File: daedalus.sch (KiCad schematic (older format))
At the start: 45 parts

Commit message: Updated schematic with MPU6050
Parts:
- added C?: 0.1uF, symbol Device:C_Small
- added C?: 2.2nF, symbol Device:C_Small
- added C? (x2): 100nF, symbol Device:C_Small
- added D?: Blue, LED_SMD:LED_0603_1608Metric, symbol Device:LED_Small
- added D?: Green, LED_SMD:LED_0603_1608Metric, symbol Device:LED_Small
- added J?: JST LiPo Input, symbol Connector:Screw_Terminal_01x02
- added J?: I2C 1 Breakout, symbol Connector_Generic:Conn_01x04
- added J? (x2): Conn_01x20_Male, symbol Connector:Conn_01x20_Male
- added R?: 1k, Resistor_SMD:R_0402_1005Metric, symbol Device:R_Small
- added R?: 1k5, Resistor_SMD:R_0402_1005Metric, symbol Device:R_Small
- added U?: MPU-6050, Sensor_Motion:InvenSense_QFN-24_4x4mm_P0.5mm, symbol Sensor_Motion:MPU-6050
- C?: value 100 nF -> 1uF
- C?: value 10 nF -> 10nF
- F?: value 500mA -> 250mA
- FB?: value 100 @ 100 MHz -> 600 @ 600MHz
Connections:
- net labels added: INT_ACC, INT_GYR, MPU_INT
- wire segments 82 -> 97
- no-connect marks 4 -> 6
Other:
- note added: "Inertial Measurement Unit"
- note added: "Pinout Connections"
- moved on the sheet: C?, D?, FB?, H?, L?, R?, SW?

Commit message: Added footprints and side headers
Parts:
- C1, C13, C14, C2, C20, C3, C4: renamed from C?; footprint (none) -> Capacitor_SMD:C_0402_1005Metric
- C19: renamed from C?; value 0.1uF -> 100nF; footprint (none) -> Capacitor_SMD:C_0402_1005Metric
- D1, D2: renamed from D?; footprint (none) -> Diode_SMD:D_SOD-123
- F1: renamed from F?; footprint (none) -> Fuse:Fuse_0603_1608Metric
- FB1: renamed from FB?; footprint (none) -> Inductor_SMD:L_0805_2012Metric
- H1, H2, H3, H4: renamed from H?; footprint (none) -> MountingHole:MountingHole_2.7mm_M2.5_Pad
- J1: renamed from J?; footprint (none) -> Connector_PinHeader_1.27mm:PinHeader_2x05_P1.27mm_Vertical_SMD
- J2: renamed from J?; footprint (none) -> Connector_USB:USB_Micro-AB_Molex_47590-0001
- J3: renamed from J?; footprint (none) -> Connector_JST:JST_PH_S2B-PH-K_1x02_P2.00mm_Horizontal
- J4: renamed from J?; footprint (none) -> Eric:JST_SH4
- J5, J6: renamed from J?; footprint (none) -> Connector_PinHeader_2.54mm:PinHeader_1x20_P2.54mm_Vertical
- L1: renamed from L?; footprint (none) -> Inductor_SMD:L_0603_1608Metric
- R1, R2, R3, R4, R5: renamed from R?; footprint (none) -> Resistor_SMD:R_0402_1005Metric
- U1: renamed from U?; footprint (none) -> Package_TO_SOT_SMD:SOT-23-6
- gave numbers to parts that had none: 29
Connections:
- net labels added: GPDIO_PC12, GPIO_PA0, GPIO_PA1, GPIO_PA10, GPIO_PA15, GPIO_PA2, GPIO_PA3, GPIO_PA4, GPIO_PA8, GPIO_PA9, GPIO_PB0, GPIO_PB1, GPIO_PB12, GPIO_PB13, GPIO_PB14, GPIO_PB15, GPIO_PB2, GPIO_PB4, GPIO_PB5, GPIO_PB8, GPIO_PB9, GPIO_PC0, GPIO_PC1, GPIO_PC10, GPIO_PC11, GPIO_PC12, GPIO_PC13, GPIO_PC14, GPIO_PC15, GPIO_PC2, GPIO_PC3, GPIO_PC4, GPIO_PC6, GPIO_PC7, GPIO_PC8, GPIO_PC9, GPIO_PD2, SPI1_MISO, SPI1_MOSI, SPI1_SCK, SPI_1_MISO, SPI_1_MOSI

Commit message: Began work adding DRV8323
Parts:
- removed C13, C14, C19: 100nF, Capacitor_SMD:C_0402_1005Metric, symbol Device:C_Small
- removed C20: 2.2nF, Capacitor_SMD:C_0402_1005Metric, symbol Device:C_Small
- removed J5, J6: Conn_01x20_Male, Connector_PinHeader_2.54mm:PinHeader_1x20_P2.54mm_Vertical, symbol Connector:Conn_01x20_Male
- removed U3: MPU-6050, Sensor_Motion:InvenSense_QFN-24_4x4mm_P0.5mm, symbol Sensor_Motion:MPU-6050
- added ?: DRV8323RH, symbol drv8323rh:DRV8323RH
- added ?: MA700, symbol ma700:MA700
- added C?: 10uF, symbol Device:C_Small
- added C?: 0.1 uF, symbol Device:C_Small
- added C?: 1 uF, symbol Device:C_Small
- added C?: 47 nF, symbol Device:C_Small
- added C?: C_Small, symbol Device:C_Small
- added C?: 22uF, symbol Device:C_Small
- added C? (x2): 0.1uF, symbol Device:C_Small
- added C?: 1uF, symbol Device:C_Small
- added D?: DIODE, symbol Simulation_SPICE:DIODE
- added L?: 22uH, symbol Device:L_Small
- added R? (x3): 10k, symbol Device:R_Small
- added R?: 54.9k, symbol Device:R_Small
- U1: symbol mp2359dj-lf-z:MP2359DJ-LF-Z -> daedalus-rescue:MP2359DJ-LF-Z-mp2359dj-lf-z
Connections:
- net labels added: +BATT, CAL, CB, ENABLE, END_A, END_B, FAULT, FB, GHA, GHB, GHC, GLA, GLB, GLC, PHASE_A, PHASE_B, PHASE_C, PWM_A, PWM_B, PWM_C, SPA, SPB, SPC, SPI_1_SCK, SPI_2_CS, SPI_2_MISO, SPI_2_MOSI, SPI_2_SCK, SW, VDS
- net labels removed: GPDIO_PC12, GPIO_PA0, GPIO_PA1, GPIO_PA10, GPIO_PA15, GPIO_PA2, GPIO_PA3, GPIO_PA8, GPIO_PA9, GPIO_PB0, GPIO_PB1, GPIO_PB12, GPIO_PB13, GPIO_PB14, GPIO_PB15, GPIO_PB2, GPIO_PB4, GPIO_PB5, GPIO_PB8, GPIO_PB9, GPIO_PC0, GPIO_PC1, GPIO_PC10, GPIO_PC11, GPIO_PC12, GPIO_PC13, GPIO_PC14, GPIO_PC15, GPIO_PC2, GPIO_PC3, GPIO_PC4, GPIO_PC6, GPIO_PC7, GPIO_PC8, GPIO_PC9, GPIO_PD2, INT_ACC, INT_GYR, MPU_INT
- wire segments 97 -> 151
- no-connect marks 6 -> 13
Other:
- note added: "DRV8323"
- note added: "Gate Driver"
- note added: "MA700GQ"
- note added: "Magnetic Encoder"
- note removed: "Inertial Measurement Unit"
- moved on the sheet: J1, J2, J3, J4, U2

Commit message: Added SPI busses, updated CubeMX files
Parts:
- added 3, U3, U5, U6, U7, U8: TPH, symbol tph:TPH
- added C26, C27, C28, C29, C30, C31, C32, C33, C34, C35, C36, C37, C38, C39, C40, C41: 10uF, 50v, symbol Device:C_Small
- added J5, J6, J7: Conn_01x01, symbol Connector_Generic:Conn_01x01
- added R17, R18, R19: 0.001, symbol Device:R_Small
- gave numbers to parts that had none: 17
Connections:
- net GPIO_PA4 is gone; now on net SPI1_NSS: U4.20 (PA4)
- net SPI1_SCK is gone; now on net GND: U4.21 (PA5)
- net SPI_1_MISO is gone; now on net SPI1_MISO: 2.29 (MODE), R13.2
- net SPI_1_MOSI is gone; now on net SPI1_MOSI: 2.30 (IDRIVE)
- net SPI_2_MISO is gone; now on net SPI2_MISO: 1.7 (MISO)
- net SPI_2_MOSI is gone; now on net SPI2_MOSI: 1.4 (MOSI)
- net SPI_2_SCK is gone; now on net SPI2_SCK: 1.12 (SCLK)
- net +BATT: now also C26.1, C27.1, C28.1, C29.1, C30.1, C31.1, C32.1, C33.1, C34.1, C35.1, C36.1, C37.1, C38.1, C39.1, C40.1, C41.1, U3.5 (D), U3.6 (D), U3.7 (D), U3.8 (D), U3.EP (D), U5.5 (D), U5.6 (D), U5.7 (D), U5.8 (D), U5.EP (D), U6.5 (D), U6.6 (D), U6.7 (D), U6.8 (D), U6.EP (D)
- net ENABLE: now also U4.17 (PA3)
- net GHA: now also U3.4 (G)
- net GHB: now also U5.4 (G)
- net GHC: now also U6.4 (G)
- net GLA: now also 3.4 (G)
- net GLB: now also U7.4 (G)
- net GLC: now also U8.4 (G)
- net GND: now also C26.2, C27.2, C28.2, C29.2, C30.2, C31.2, C32.2, C33.2, C34.2, C35.2, C36.2, C37.2, C38.2, C39.2, C40.2, C41.2, R17.2, R18.2, R19.2
- net LED_STATUS: now also U4.50 (PA15); no longer U4.16 (PA2)
- net PHASE_A: now also 3.5 (D), 3.6 (D), 3.7 (D), 3.8 (D), 3.EP (D), J5.1 (Pin_1), U3.1 (S), U3.2 (S), U3.3 (S)
- net PHASE_B: now also J6.1 (Pin_1), U5.1 (S), U5.2 (S), U5.3 (S), U7.5 (D), U7.6 (D), U7.7 (D), U7.8 (D), U7.EP (D)
- net PHASE_C: now also J7.1 (Pin_1), U6.1 (S), U6.2 (S), U6.3 (S), U8.5 (D), U8.6 (D), U8.7 (D), U8.8 (D), U8.EP (D)
- net PWM_A: now also U4.14 (PA0)
- net PWM_B: now also U4.15 (PA1)
- net PWM_C: now also U4.16 (PA2)
- net SPA: now also 3.1 (S), 3.2 (S), 3.3 (S), R17.1
- net SPB: now also R18.1, U7.1 (S), U7.2 (S), U7.3 (S)
- net SPC: now also R19.1, U8.1 (S), U8.2 (S), U8.3 (S)
- net SPI2_MISO: now reaches U4.10 (PC2)
- net SPI2_MOSI: now reaches U4.11 (PC3)
- net SPI2_SCK: now reaches U4.34 (PB13)
- net SPI1_NSS: now reaches 2.32 (GAIN)
- net SPI_2_CS renamed SPI2_CS
- no-connect marks 13 -> 14
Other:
- note added: "DAEDALUS"
- note added: "Motor Interface"
- moved on the sheet: C13, C14, C19, C20, C21, C22, C23, C24, C25, D6, J1, J2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

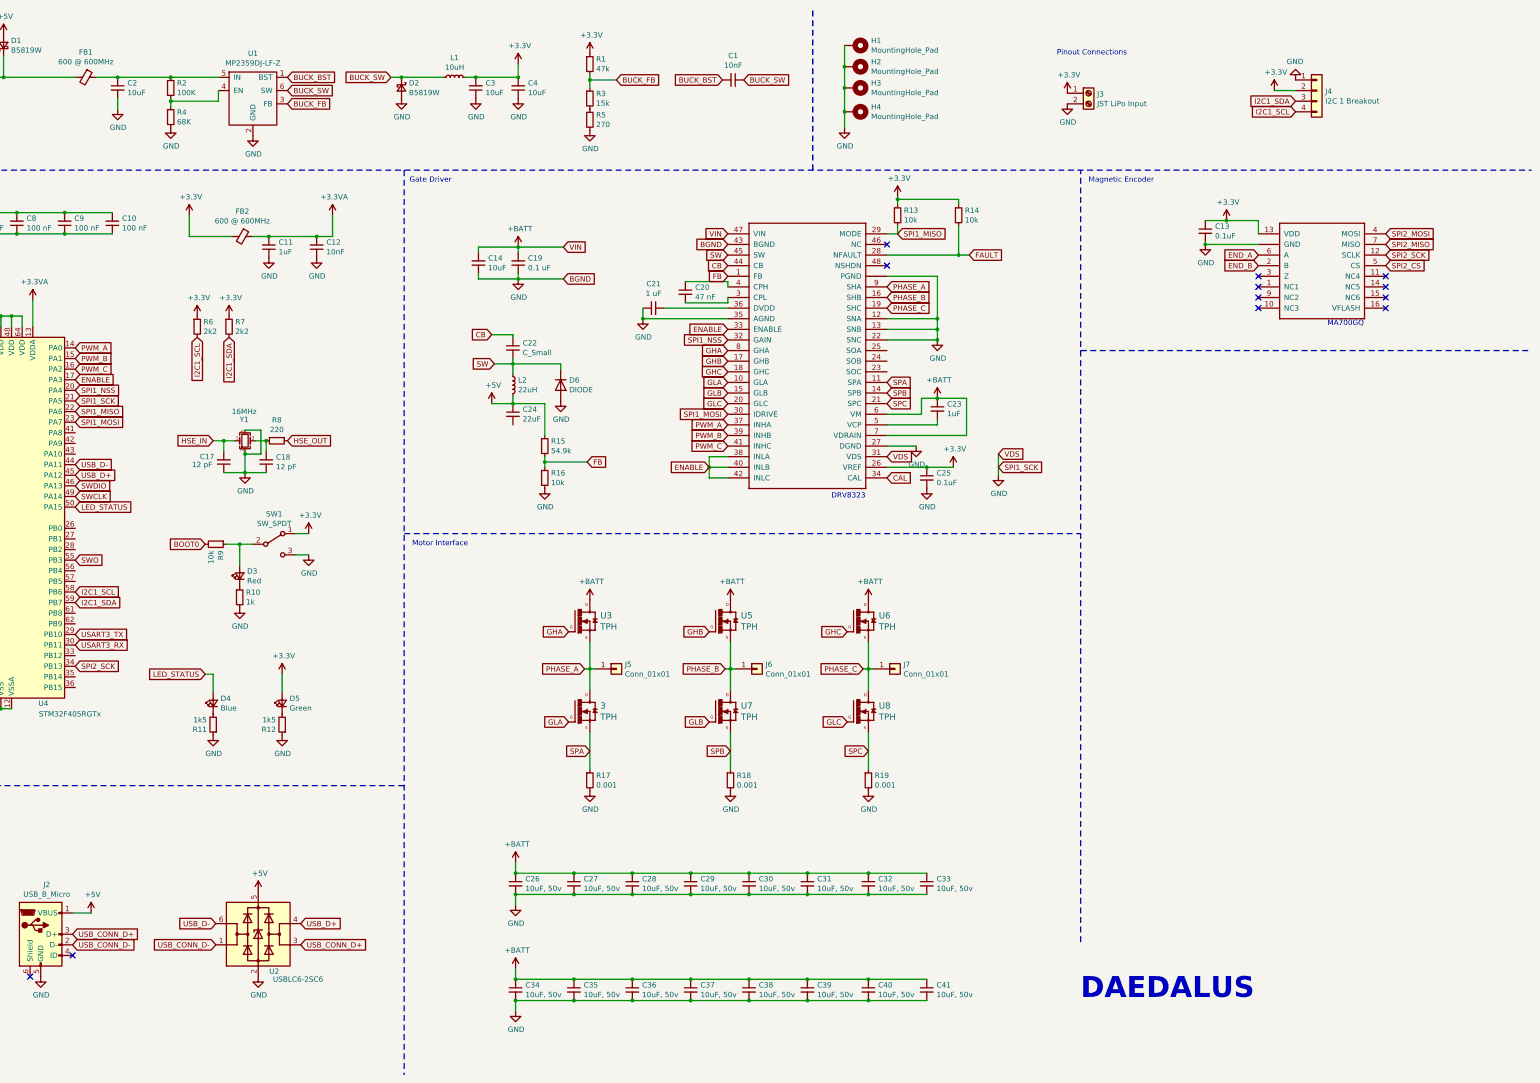
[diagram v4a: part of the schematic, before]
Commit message: Added CAN interface, fixed value labels
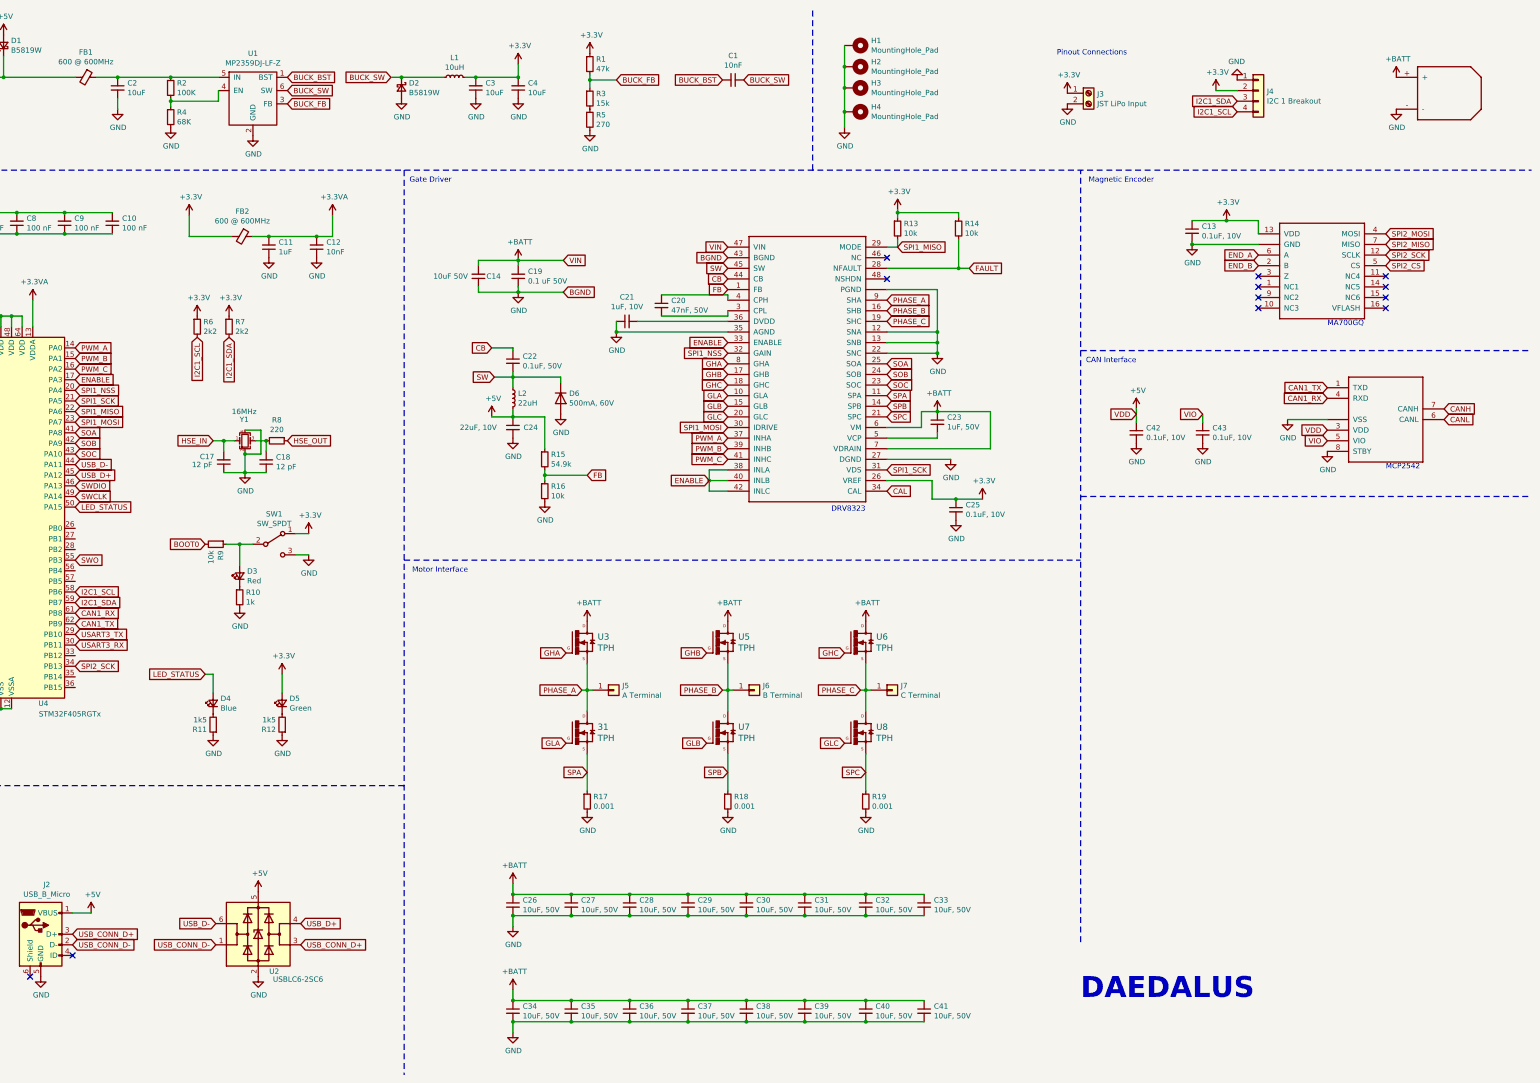
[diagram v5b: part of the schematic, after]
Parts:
- added 1?: XT30, symbol xt30:XT30
- added 2?: MCP2542, symbol mcp2542:MCP2542
- added C42, C43: 0.1uF, 10V, symbol Device:C_Small
- C13, C25: value 0.1uF -> 0.1uF, 10V
- C14: value 10uF -> 10uF 50V
- C19: value 0.1 uF -> 0.1 uF 50V
- C20: value 47 nF -> 47nF, 50V
- C21: value 1 uF -> 1uF, 10V
- C22: value C_Small -> 0.1uF, 50V
- C23: value 1uF -> 1uF, 50V
- C24: value 22uF -> 22uF, 10V
- C26, C27, C28, C29, C30, C31, C32, C33, C34, C35, C36, C37, C38, C39, C40, C41: value 10uF, 50v -> 10uF, 50V
- D6: value DIODE -> 500mA, 60V
- J5: value Conn_01x01 -> A Terminal
- J6: value Conn_01x01 -> B Terminal
- J7: value Conn_01x01 -> C Terminal
- renumbered 1 to 11, 2 to 21, 3 to 31
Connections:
- net +5V: now also 2?.3 (VDD), C42.1
- net +BATT: now also 1?.+
- net GND: now also C24.2, 1?.-, 2?.2 (VSS), 2?.8 (STBY), 2?.9 (VSS), C42.2, C43.2; no longer 21.31 (VDS), U4.21 (PA5)
- net SOA: now reaches U4.41 (PA8)
- net SOA: now also 21.25 (SOA)
- net SOB: now reaches U4.42 (PA9)
- net SOB: now also 21.24 (SOB)
- net SOC: now reaches U4.43 (PA10)
- net SOC: now also 21.23 (SOC)
- net CAN1_RX: now reaches U4.61 (PB8)
- net CAN1_RX: now also 2?.4 (RXD)
- net CAN1_TX: now reaches U4.62 (PB9)
- net CAN1_TX: now also 2?.1 (TXD)
- new net CANH: 2?.7 (CANH)
- new net CANL: 2?.6 (CANL)
- new net SPI1_SCK: 21.31 (VDS), U4.21 (PA5)
- new net VIO: 2?.5 (VIO), C43.1
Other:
- note added: "CAN Interface"
- note added: "MCP2542"
- moved on the sheet: 31, C13, C14, C19, C20, C21, C22, C23, C24, C25, C26, C27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

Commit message: Updated buck regulator output, removed battery connector
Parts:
- removed D6: 500mA, 60V, symbol Simulation_SPICE:DIODE
- removed J3: JST LiPo Input, Connector_JST:JST_PH_S2B-PH-K_1x02_P2.00mm_Horizontal, symbol Connector:Screw_Terminal_01x02
- added C28, C29, C30, C31, C32: C_Small, symbol Device:C_Small
- added D3: 500mA, 60V, Diode_SMD:D_SOD-123, symbol Device:D_Schottky_Small
- added J2, J3: CAN Bus, symbol Connector_Generic:Conn_01x03
- gave numbers to parts that had none: 2
- renumbered C13 to C11, C11 to C12, C12 to C13, C19 to C15, C20 to C16, C21 to C17, C22 to C18, C15 to C19, C16 to C20, C23 to C21, C24 to C22, C42 to C23, C43 to C24, C17 to C25, C18 to C26, C25 to C27, C26 to C33, C27 to C34, C28 to C35, C29 to C36, C30 to C37, C31 to C38, C32 to C39, C33 to C40, C34 to C41, C35 to C42, C36 to C43, C37 to C44, C38 to C45, C39 to C46, C40 to C47, C41 to C48, D3 to D4, D4 to D5, D5 to D6, J4 to J1, J5 to J4, J6 to J5, J7 to J6, J1 to J7, J2 to J8, R8 to R10, R15 to R11, R16 to R12, R9 to R13, R10 to R14, R11 to R15, R12 to R16, R13 to R6, R14 to R7, R6 to R8, R7 to R9, 31 to U10, U7 to U11, U8 to U12, U2 to U13, U1 to U2, 11 to U3, 21 to U4, U4 to U6, U3 to U7, U5 to U8, U6 to U9
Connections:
- net +3V3: now also C23.1, U5.3 (VDD)
- net +5V: no longer C22.1, C23.1, L2.2, R11.1, U5.3 (VDD)
- net +BATT: now also C28.1, C29.1, C30.1, C31.1, C32.1
- net CANH: now also J2.1 (Pin_1), J3.1 (Pin_1)
- net CANL: now also J2.2 (Pin_2), J3.2 (Pin_2)
- net GND: now also C28.2, C29.2, C30.2, C31.2, C32.2, D3.2 (A), J2.3 (Pin_3), J3.3 (Pin_3)
- net SW: now also D3.1 (K)
- net VCC renamed +5VD
- net +5VD: now also C22.1, L2.2, R11.1
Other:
- note added: "+5VD refers to the output of the buck regulator on the DRV\n+5V refers to the voltage from using the USB port"
- note added: "Buck\nRegulated\nOutput"
- note added: "Power and Mounting Points"
- note added: "V_o=5V=0.765V*(1+(R1/R2))"
- moved on the sheet: C14, C15, C16, C17, C18, C21, C22, C27, H1, H2, H3, H4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

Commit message: Updated schematic, added footprints, added BOM
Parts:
- removed C28, C29, C30, C31, C32: C_Small, symbol Device:C_Small
- added D1: B5819W, Diode_SMD:D_SOD-123, symbol Device:D_Schottky_Small
- added J4: I2C 1 Breakout, Connector_JST:JST_PH_S4B-PH-K_1x04_P2.00mm_Horizontal, symbol Connector_Generic:Conn_01x04
- added U2: XT30, daedalus_kicad_lib:XT30_HORIZONTAL, symbol xt30:XT30
- C11, C23, C24: footprint (none) -> Capacitor_SMD:C_0603_1608Metric
- C14: footprint (none) -> Capacitor_SMD:C_1206_3216Metric
- C15, C16, C17, C18, C21, C22, C27: footprint (none) -> Capacitor_SMD:C_0402_1005Metric
- C28: renamed from C33; footprint (none) -> Capacitor_SMD:C_1206_3216Metric
- C29: renamed from C34; footprint (none) -> Capacitor_SMD:C_1206_3216Metric
- C30: renamed from C35; footprint (none) -> Capacitor_SMD:C_1206_3216Metric
- C31: renamed from C36; footprint (none) -> Capacitor_SMD:C_1206_3216Metric
- C32: renamed from C37; footprint (none) -> Capacitor_SMD:C_1206_3216Metric
- C33: renamed from C38; footprint (none) -> Capacitor_SMD:C_1206_3216Metric
- C34: renamed from C39; footprint (none) -> Capacitor_SMD:C_1206_3216Metric
- C35: renamed from C40; footprint (none) -> Capacitor_SMD:C_1206_3216Metric
- C36: renamed from C41; footprint (none) -> Capacitor_SMD:C_1206_3216Metric
- C37: renamed from C42; footprint (none) -> Capacitor_SMD:C_1206_3216Metric
- C38: renamed from C43; footprint (none) -> Capacitor_SMD:C_1206_3216Metric
- C39: renamed from C44; footprint (none) -> Capacitor_SMD:C_1206_3216Metric
- C40: renamed from C45; footprint (none) -> Capacitor_SMD:C_1206_3216Metric
- C41: renamed from C46; footprint (none) -> Capacitor_SMD:C_1206_3216Metric
- C42: renamed from C47; footprint (none) -> Capacitor_SMD:C_1206_3216Metric
- C43: renamed from C48; footprint (none) -> Capacitor_SMD:C_1206_3216Metric
- J1: renamed from J2; footprint (none) -> Connector_JST:JST_PH_S3B-PH-K_1x03_P2.00mm_Horizontal
- J2: renamed from J3; footprint (none) -> Connector_JST:JST_PH_S3B-PH-K_1x03_P2.00mm_Horizontal
- J3: renamed from J1; footprint Eric:JST_SH4 -> Connector_JST:JST_PH_S4B-PH-K_1x04_P2.00mm_Horizontal
- J5: renamed from J4; footprint (none) -> daedalus_kicad_lib:18_AWG_PAD
- J6: renamed from J5; footprint (none) -> daedalus_kicad_lib:18_AWG_PAD
- J7: renamed from J6; footprint (none) -> daedalus_kicad_lib:18_AWG_PAD
- L2: footprint (none) -> Inductor_SMD:L_0603_1608Metric
- R11, R12, R17, R18, R19, R6, R7: footprint (none) -> Resistor_SMD:R_0402_1005Metric
- U1: footprint (none) -> daedalus_kicad_lib:XT30_HORIZONTAL
- U10: renamed from U9; footprint (none) -> daedalus_kicad_lib:TRANS_TPH5900CNH,L1Q
- U11: renamed from U10; footprint (none) -> daedalus_kicad_lib:TRANS_TPH5900CNH,L1Q
- U12: renamed from U11; footprint (none) -> daedalus_kicad_lib:TRANS_TPH5900CNH,L1Q
- U13: renamed from U12; footprint (none) -> daedalus_kicad_lib:TRANS_TPH5900CNH,L1Q
- U4: renamed from U3; footprint (none) -> daedalus_kicad_lib:QFN16
- U5: renamed from U4; footprint (none) -> daedalus_kicad_lib:QFN50P700X700X90-49N
- U6: renamed from U5; footprint (none) -> daedalus_kicad_lib:TDFN
- U8: renamed from U7; footprint (none) -> daedalus_kicad_lib:TRANS_TPH5900CNH,L1Q
- U9: renamed from U8; footprint (none) -> daedalus_kicad_lib:TRANS_TPH5900CNH,L1Q
- renumbered D1 to D2, D2 to D3, D3 to D4, D4 to D5, D5 to D6, D6 to D7, J7 to J8, J8 to J9, U13 to U14, U2 to U3, U6 to U7
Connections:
- net +3V3: now also J4.2 (Pin_2)
- net +5VD: now also D1.2 (A); no longer F1.2
- net +BATT: now also U2.+
- net GND: now also J4.1 (Pin_1), U2.-
- net I2C1_SCL: now also J4.4 (Pin_4)
- net I2C1_SDA: now also J4.3 (Pin_3)
- new net: D1.1 (K), F1.2
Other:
- note added: "2x all busses: input and daisy chain"
- note added: "Caps for Input Voltage"
- note added: "Caps leading directly to MOSFETS"
- note added: "Two XT30 plugs: power in and daisy chaining"
- moved on the sheet: D2, F1, J1, J2, J3, Q1

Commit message: Began board layout
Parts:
- added R10, R11: 2k2, Resistor_SMD:R_0402_1005Metric, symbol Device:R_Small
- renumbered R10 to R12, R11 to R13, R12 to R14, R13 to R15, R14 to R16, R15 to R17, R16 to R18, R17 to R19, R18 to R20, R19 to R21
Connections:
- net +3V3: now also R10.1, R11.1
- net I2C1_SCL: now also R10.2
- net I2C1_SDA: now also R11.2
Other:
- note added: "Caps for Input voltage and leading to MOSFETS"
- note removed: "Caps for Input Voltage"
- note removed: "Caps leading directly to MOSFETS"
